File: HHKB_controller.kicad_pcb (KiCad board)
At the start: 2 copper layers, 141.5 x 36 mm, 96 parts, among them CN1 CONN_15, CN2 CONN_13, J1 USB_mini_micro_B, P1 GND, P10 CONN_1, P100 CONN_2, P11 CONN_1, P110 CONN_1, P111 CONN_1, P112 CONN_1, P113 CONN_1, P114 CONN_1, P115 CONN_1, P12 CONN_1, P130 CONN_1, P131 CONN_1, P2 D+, P3 D-, P4 VUSB, P5 PD1, P6 PD0, P7 GND, P8 CONN_3X2, P9 CONN_1, Q1 N, Q2 N, Q3 N, Q5 P, SW1 SW_PUSH, SW2 SW_DPDT, U1 ATMEGA32U4, U2 TAR5SB33, U3 NCP1402, U4 MCP73831, U5 RN42, X1 16MHz

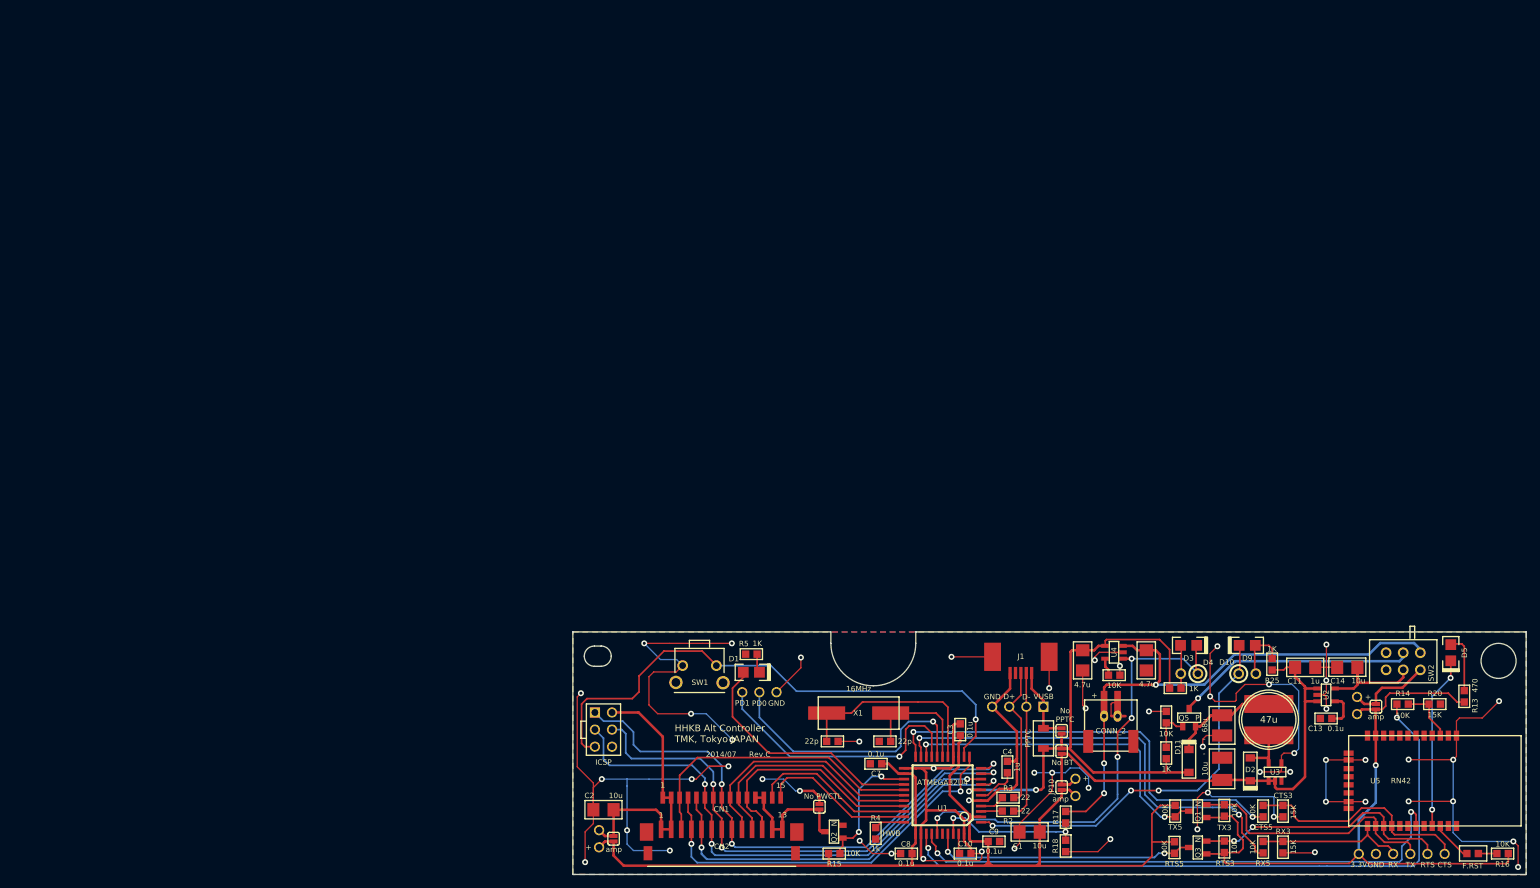
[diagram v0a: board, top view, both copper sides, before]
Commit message: SLP3.mod added, components added to board
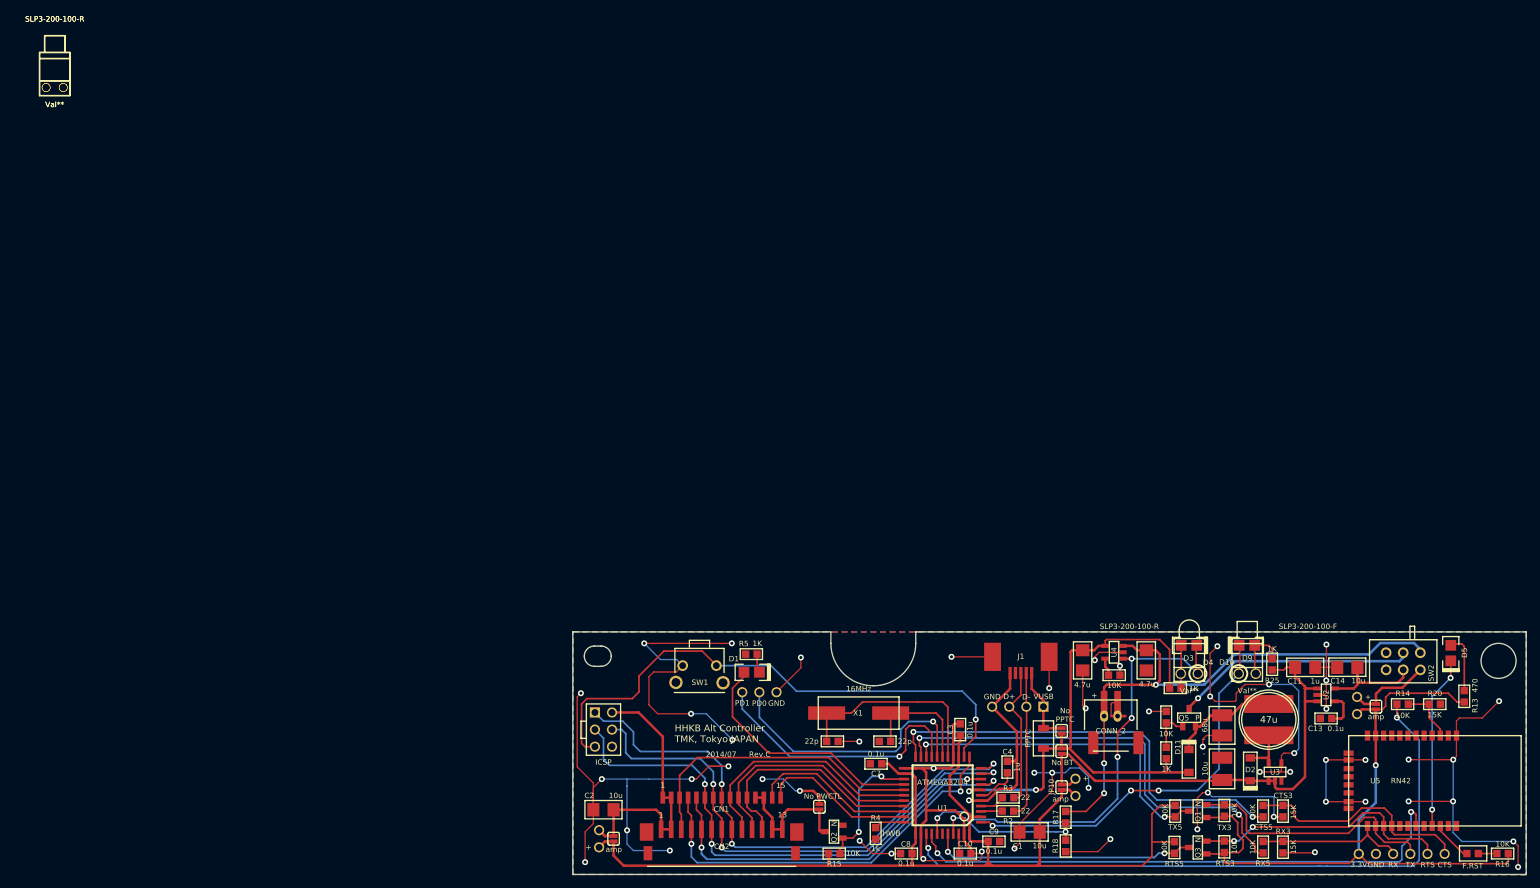
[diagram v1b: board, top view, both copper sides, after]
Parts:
- added SLP3-200-100-F: Val**, SLP3-200-100-F, F.Cu at (177.0, 87.0)
- added SLP3-200-100-R (x2): Val**, SLP3-200-100-F, F.Cu at (0.00, 0.00)
- added SLP3-200-100-R: Val**, SLP3-200-100-R, F.Cu at (168.4, 87.0)
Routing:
- net Net-(D3-Pad1): track 6.40 -> 0.00 mm
- net (no net): track 0.00 -> 6.40 mm
